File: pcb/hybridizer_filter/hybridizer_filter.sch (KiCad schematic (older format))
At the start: 107 parts, among them P1 HEADER_02X07_SMD, P2 HEADER_02X05_SMD, P3 HEADER_02X05_SMD, U1 VA, U11 VA, U13 VA, U15 DRV103, U16 DRV103, U17 DRV103, U18 DRV103, U19 DRV103, U20 DRV103, U21 DRV103, U22 DRV103, U23 OA, U24 OA, U25 OA, U26 OA, U27 OA, U28 OA, U29 OA, U3 VA, U5 VA, U7 VA, U9 VA

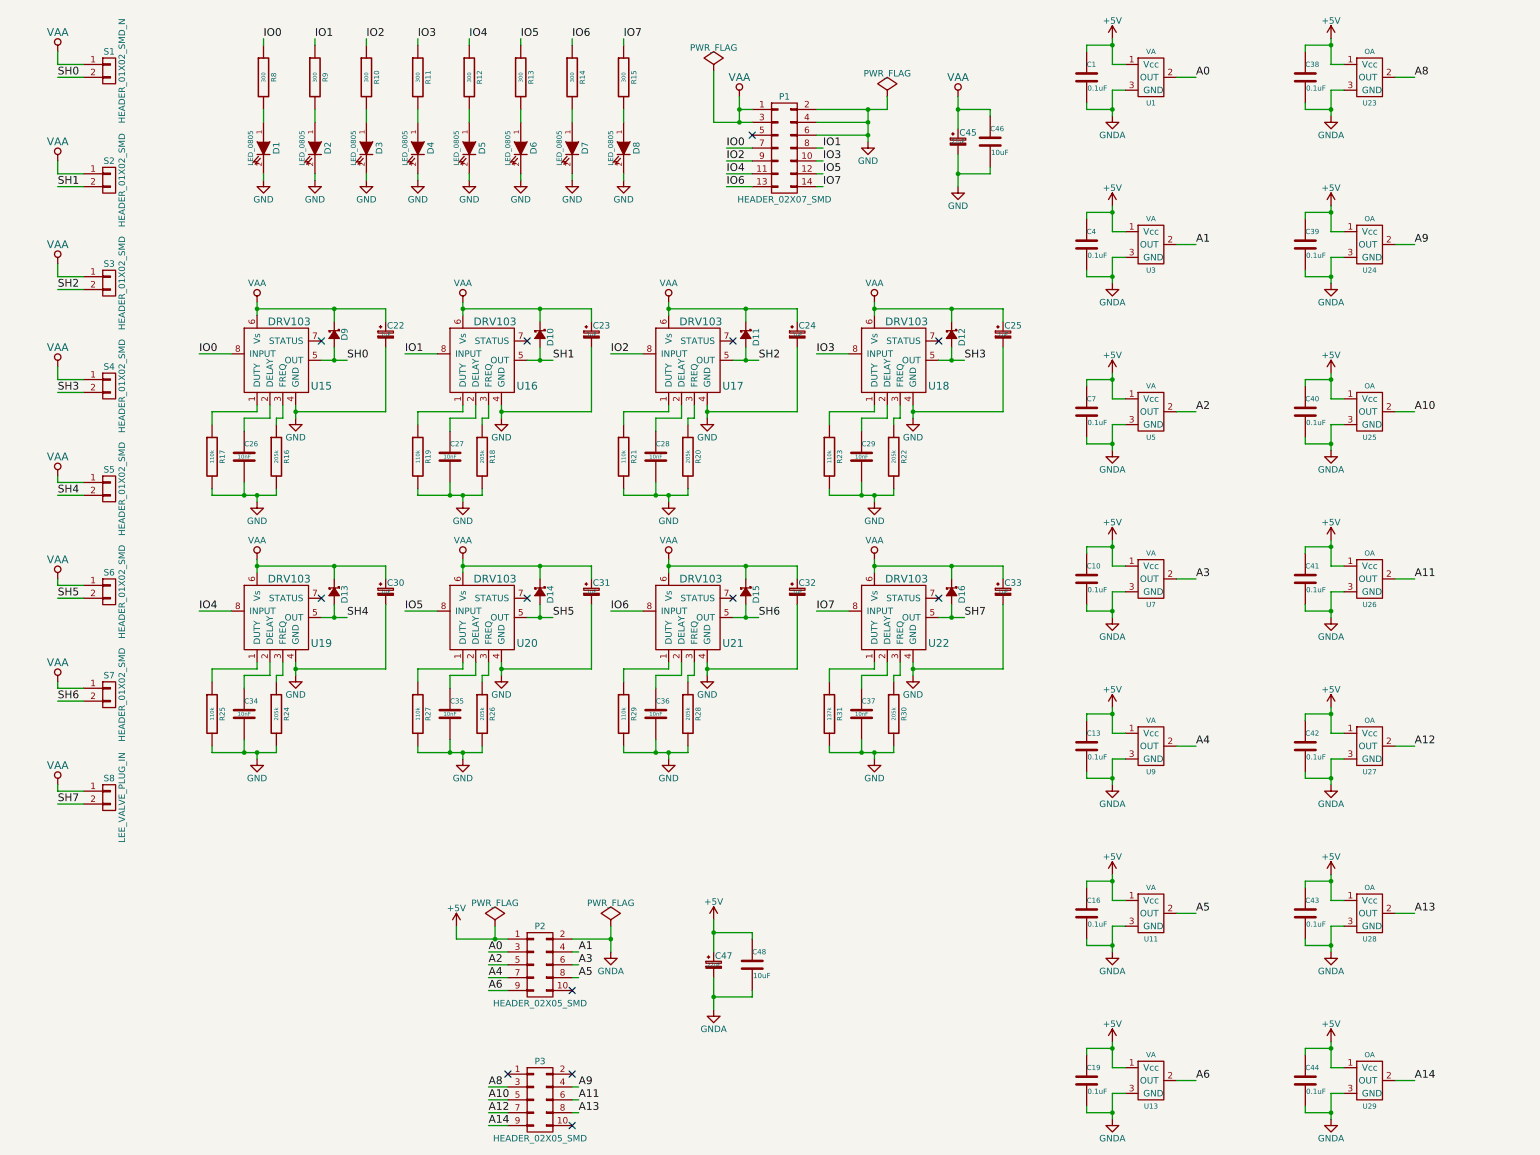
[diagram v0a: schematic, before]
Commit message: Initial design of hybridizer_filter pcb.
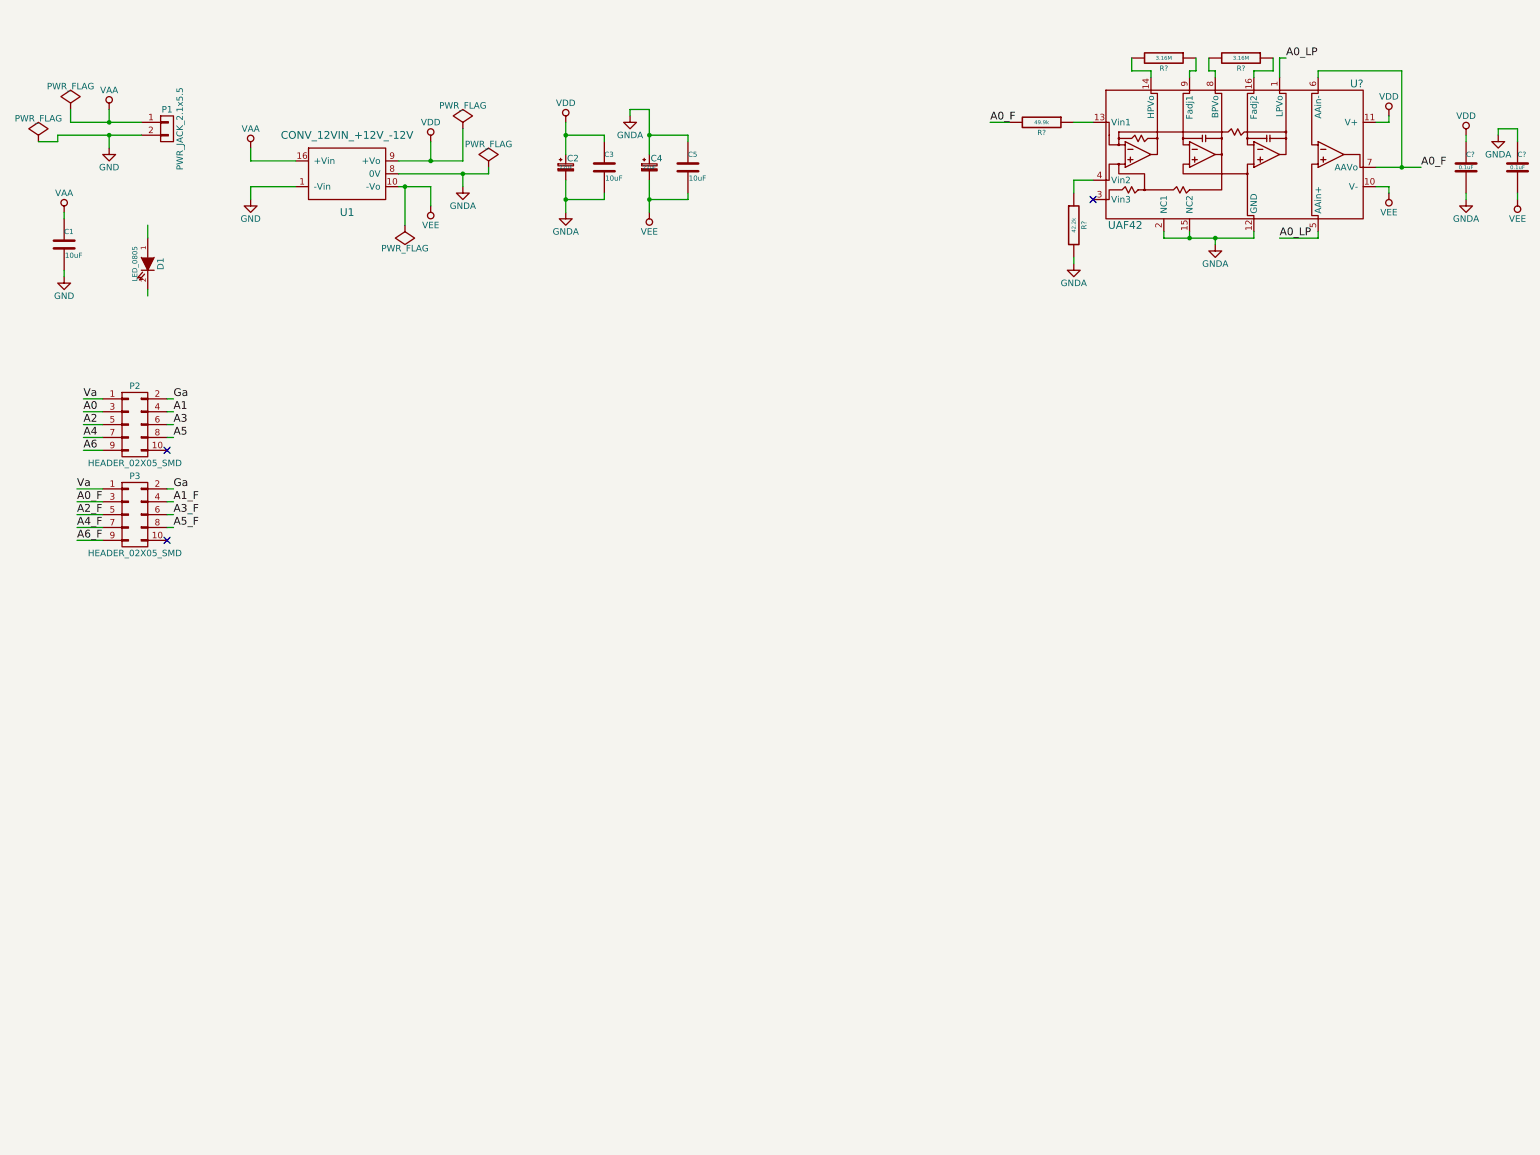
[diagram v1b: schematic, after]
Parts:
- removed C1, C10, C13, C16, C19, C38, C39, C4, C40, C41, C42, C43, C44, C7: 0.1uF, hybridizer_filter:SM1210, symbol 0.1uF
- removed C22, C23, C24, C25, C30, C31, C32, C33: 1uF, hybridizer_filter:SM0805_POL_L, symbol 1uF_0805_POL
- removed C26, C27, C28, C29, C34, C35, C36, C37: 10nF, hybridizer_filter:SM0402, symbol 10nF_0402
- removed C45: 22uF, hybridizer_filter:SM1210_POL, symbol 22uF_1210_POL
- removed C46: 10uF, hybridizer_filter:SM1210, symbol 10uF
- removed D10, D11, D12, D13, D14, D15, D16, D9: diode_schottky_20V_1A, hybridizer_filter:SM0805_POL, symbol diode_schottky_20V_1A
- removed D2, D3, D4, D5, D6, D7, D8: LED_0805, hybridizer_filter:LED0805, symbol LED_0805
- removed P1: HEADER_02X07_SMD, hybridizer_filter:HEADER_02x07_SMD, symbol HEADER_02X07_SMD
- removed R10, R11, R12, R13, R14, R15, R8, R9: 300, hybridizer_filter:SM0402, symbol 300_0402
- removed R16, R18, R20, R22, R24, R26, R28, R30: 205k, hybridizer_filter:SM0402, symbol 205k_0402
- removed R17, R19, R21, R23, R25, R27, R29: 110k, hybridizer_filter:SM0402, symbol 110k_0402
- removed R31: 137k, hybridizer_filter:SM0402, symbol 137k_0402
- removed S1: HEADER_01X02_SMD_N, hybridizer_filter:Header_2_Pin_SMD_N, symbol HEADER_01X02_SMD_N
- removed S2, S3, S4, S5, S6, S7: HEADER_01X02_SMD, hybridizer_filter:Header_2_Pin_SMD, symbol HEADER_01X02_SMD
- removed S8: LEE_VALVE_PLUG_IN, hybridizer_filter:LEE_VALVE_PLUG_IN, symbol LEE_VALVE_PLUG_IN
- removed U1, U11, U13, U3, U5, U7, U9: VA, hybridizer_filter:SOT-23-3, symbol HALL_DRV5053_VA_-9mT
- removed U15, U16, U17, U18, U19, U20, U21, U22: DRV103, hybridizer_filter:SOIC_8, symbol DRV103
- removed U23, U24, U25, U26, U27, U28, U29: OA, hybridizer_filter:SOT-23-3, symbol HALL_DRV5053_OA_-73mT
- added C1, C5: 10uF, hybridizer_filter:SM1210, symbol 10uF
- added C4: 22uF, hybridizer_filter:SM1210_POL, symbol 22uF_1210_POL
- added C? (x2): 0.1uF, hybridizer_filter:SM0805, symbol 0.1uF_0805
- added P1: PWR_JACK_2.1x5.5, hybridizer_filter:DCJACK_2PIN_HIGHCURRENT, symbol PWR_JACK_2.1x5.5
- added R?: 42.2k, hybridizer_filter:SM0805, symbol 42.2k_0805
- added R?: 49.9k, hybridizer_filter:SM0805, symbol 49.9k_0805
- added R? (x2): 3.16M, hybridizer_filter:SM0805, symbol 3.16M_0805
- added U1: CONV_12VIN_+12V_-12V, hybridizer_filter:XP_DC_DC_ISP, symbol CONV_12VIN_+12V_-12V
- added U?: UAF42, hybridizer_filter:SOIC_16, symbol UAF42
- renumbered C47 to C2, C48 to C3
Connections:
- net GND: now also C1.2, P1.2 (P2), U1.1 (-Vin); no longer D1.2 (K)
- net GNDA: now also C4.1, C5.1, C?.1, C?.2, R?.2, U1.8 (0V), U?.12 (GND), U?.15 (NC2), U?.2 (NC1); no longer P2.2 (P2)
- net VAA: now also C1.1, P1.1 (P1), U1.16 (+Vin)
- net Va: now reaches P3.1 (P1)
- net Va: now also P2.1 (P1)
- net Ga: now reaches P3.2 (P2)
- net Ga: now also P2.2 (P2)
- net +5V renamed VDD
- net VDD: now also C?.1, U1.9 (+Vo), U?.11 (V+); no longer P2.1 (P1)
- net A10 renamed A2_F
- net A11 renamed A3_F
- net A12 renamed A4_F
- net A13 renamed A5_F
- net A14 renamed A6_F
- net A8 renamed A0_F
- net A0_F: now also R?.2, U?.6 (AAin-), U?.7 (AAVo)
- net A9 renamed A1_F
- new net: R?.1, U?.13 (Vin1)
- new net: R?.2, U?.14 (HPVo)
- new net: R?.1, U?.16 (Fadj2)
- new net: R?.1, U?.4 (Vin2)
- new net: R?.2, U?.8 (BPVo)
- new net: R?.1, U?.9 (Fadj1)
- new net A0_LP: U?.1 (LPVo), U?.5 (AAin+)
- new net VEE: C4.2, C5.2, C?.2, U1.10 (-Vo), U?.10 (V-)
- no-connect marks 13 -> 3
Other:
- moved on the sheet: C2, C3, D1, P2, P3

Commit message: Progress towards hybridizer_filter v1.0.
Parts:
- removed U1: CONV_12VIN_+12V_-12V, hybridizer_filter:XP_DC_DC_ISP, symbol CONV_12VIN_+12V_-12V
- added C10, C11, C12, C13, C14, C15, C16, C17, C18, C19, C20, C21, C22, C23, C24, C25, C26, C27, C28, C29, C30, C31, C32, C33, C8, C9: 0.1uF, hybridizer_filter:SM0805, symbol 0.1uF_0805
- added P4, P5: HEADER_02X05_SMD, hybridizer_filter:HEADER_02x05_SMD, symbol HEADER_02X05_SMD
- added R1: 1k, hybridizer_filter:SM0805, symbol 1k_0805
- added R10, R11, R14, R15, R18, R19, R22, R23, R26, R27, R30, R31, R34, R35, R38, R39, R42, R43, R46, R47, R50, R51, R54, R55, R6, R7: 3.16M, hybridizer_filter:SM0805, symbol 3.16M_0805
- added R12, R16, R20, R24, R28, R32, R36, R40, R44, R48, R52, R56, R8: 49.9k, hybridizer_filter:SM0805, symbol 49.9k_0805
- added R13, R17, R21, R25, R29, R33, R37, R41, R45, R49, R53, R57, R9: 42.2k, hybridizer_filter:SM0805, symbol 42.2k_0805
- added U1: CONV_+9V_-9V_SIP8, hybridizer_filter:SIP8_RECOM, symbol CONV_+9V_-9V_SIP8
- added U10, U11, U12, U13, U14, U15, U3, U4, U5, U6, U7, U8, U9: UAF42, hybridizer_filter:SOIC_16, symbol UAF42
- gave numbers to parts that had none: 7
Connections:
- net Ga is gone; now on net GNDA: P2.2 (P2), P3.2 (P2)
- net A0: now also R4.2
- net A0_F: no longer R4.2
- net A1: now also R8.2
- net A1_F: now also U3.6 (AAin-), U3.7 (AAVo)
- net A2: now also R12.2
- net A2_F: now also U4.6 (AAin-), U4.7 (AAVo)
- net A3: now also R16.2
- net A3_F: now also U5.6 (AAin-), U5.7 (AAVo)
- net A4: now also R20.2
- net A4_F: now also U6.6 (AAin-), U6.7 (AAVo)
- net A5: now also R24.2
- net A5_F: now also U7.6 (AAin-), U7.7 (AAVo)
- net A6: now also R28.2
- net A6_F: now also U8.6 (AAin-), U8.7 (AAVo)
- net GND: now also D1.2 (K), U1.1 (-Vin)
- net GNDA: now also C10.2, C11.1, C12.2, C13.1, C14.2, C15.1, C16.2, C17.1, C18.2, C19.1, C20.2, C21.1, C22.2, C23.1, C24.2, C25.1, C26.2, C27.1, C28.2, C29.1, C30.2, C31.1, C32.2, C33.1, C8.2, C9.1, R13.2, R17.2, R21.2, R25.2, R29.2, R33.2, R37.2, R41.2, R45.2, R49.2, R53.2, R57.2, R9.2, U1.7 (COM), U10.12 (GND), U10.15 (NC2), U10.2 (NC1), U11.12 (GND), U11.15 (NC2), U11.2 (NC1), U12.12 (GND), U12.15 (NC2), U12.2 (NC1), U13.12 (GND), U13.15 (NC2), U13.2 (NC1), U14.12 (GND), U14.15 (NC2), U14.2 (NC1), U15.12 (GND), U15.15 (NC2), U15.2 (NC1), U3.12 (GND), U3.15 (NC2), U3.2 (NC1), U4.12 (GND), U4.15 (NC2), U4.2 (NC1), U5.12 (GND), U5.15 (NC2), U5.2 (NC1), U6.12 (GND), U6.15 (NC2), U6.2 (NC1), U7.12 (GND), U7.15 (NC2), U7.2 (NC1), U8.12 (GND), U8.15 (NC2), U8.2 (NC1), U9.12 (GND), U9.15 (NC2), U9.2 (NC1)
- net VAA: now also R1.1, U1.2 (+Vin)
- net VDD: now also C10.1, C12.1, C14.1, C16.1, C18.1, C20.1, C22.1, C24.1, C26.1, C28.1, C30.1, C32.1, C8.1, U1.6 (+Vo), U10.11 (V+), U11.11 (V+), U12.11 (V+), U13.11 (V+), U14.11 (V+), U15.11 (V+), U3.11 (V+), U4.11 (V+), U5.11 (V+), U6.11 (V+), U7.11 (V+), U8.11 (V+), U9.11 (V+)
- net VEE: now also C11.2, C13.2, C15.2, C17.2, C19.2, C21.2, C23.2, C25.2, C27.2, C29.2, C31.2, C33.2, C9.2, U1.8 (-Vo), U10.10 (V-), U11.10 (V-), U12.10 (V-), U13.10 (V-), U14.10 (V-), U15.10 (V-), U3.10 (V-), U4.10 (V-), U5.10 (V-), U6.10 (V-), U7.10 (V-), U8.10 (V-), U9.10 (V-)
- net at D1.1 (A): now also R1.2
- new net: R8.1, U3.13 (Vin1)
- new net: R6.2, U3.14 (HPVo)
- new net: R7.1, U3.16 (Fadj2)
- new net: R9.1, U3.4 (Vin2)
- new net: R7.2, U3.8 (BPVo)
- new net: R6.1, U3.9 (Fadj1)
- new net: R12.1, U4.13 (Vin1)
- new net: R10.2, U4.14 (HPVo)
- new net: R11.1, U4.16 (Fadj2)
- new net: R13.1, U4.4 (Vin2)
- new net: R11.2, U4.8 (BPVo)
- new net: R10.1, U4.9 (Fadj1)
- new net: R16.1, U5.13 (Vin1)
- new net: R14.2, U5.14 (HPVo)
- new net: R15.1, U5.16 (Fadj2)
- new net: R17.1, U5.4 (Vin2)
- new net: R15.2, U5.8 (BPVo)
- new net: R14.1, U5.9 (Fadj1)
- new net: R20.1, U6.13 (Vin1)
- new net: R18.2, U6.14 (HPVo)
- new net: R19.1, U6.16 (Fadj2)
- new net: R21.1, U6.4 (Vin2)
- new net: R19.2, U6.8 (BPVo)
- new net: R18.1, U6.9 (Fadj1)
- new net: R24.1, U7.13 (Vin1)
- new net: R22.2, U7.14 (HPVo)
- new net: R23.1, U7.16 (Fadj2)
- new net: R25.1, U7.4 (Vin2)
- new net: R23.2, U7.8 (BPVo)
- new net: R22.1, U7.9 (Fadj1)
- new net: R28.1, U8.13 (Vin1)
- new net: R26.2, U8.14 (HPVo)
- new net: R27.1, U8.16 (Fadj2)
- new net: R29.1, U8.4 (Vin2)
- new net: R27.2, U8.8 (BPVo)
- new net: R26.1, U8.9 (Fadj1)
- new net: R32.1, U9.13 (Vin1)
- new net: R30.2, U9.14 (HPVo)
- new net: R31.1, U9.16 (Fadj2)
- new net: R33.1, U9.4 (Vin2)
- new net: R31.2, U9.8 (BPVo)
- new net: R30.1, U9.9 (Fadj1)
- new net: R36.1, U10.13 (Vin1)
- new net: R34.2, U10.14 (HPVo)
- new net: R35.1, U10.16 (Fadj2)
- new net: R37.1, U10.4 (Vin2)
- new net: R35.2, U10.8 (BPVo)
- new net: R34.1, U10.9 (Fadj1)
- new net: R40.1, U11.13 (Vin1)
- new net: R38.2, U11.14 (HPVo)
- new net: R39.1, U11.16 (Fadj2)
- new net: R41.1, U11.4 (Vin2)
- new net: R39.2, U11.8 (BPVo)
- new net: R38.1, U11.9 (Fadj1)
- new net: R44.1, U12.13 (Vin1)
- new net: R42.2, U12.14 (HPVo)
- new net: R43.1, U12.16 (Fadj2)
- new net: R45.1, U12.4 (Vin2)
- new net: R43.2, U12.8 (BPVo)
- new net: R42.1, U12.9 (Fadj1)
- new net: R48.1, U13.13 (Vin1)
- new net: R46.2, U13.14 (HPVo)
- new net: R47.1, U13.16 (Fadj2)
- new net: R49.1, U13.4 (Vin2)
- new net: R47.2, U13.8 (BPVo)
- new net: R46.1, U13.9 (Fadj1)
- new net: R52.1, U14.13 (Vin1)
- new net: R50.2, U14.14 (HPVo)
- new net: R51.1, U14.16 (Fadj2)
- new net: R53.1, U14.4 (Vin2)
- new net: R51.2, U14.8 (BPVo)
- new net: R50.1, U14.9 (Fadj1)
- new net: R56.1, U15.13 (Vin1)
- new net: R54.2, U15.14 (HPVo)
- new net: R55.1, U15.16 (Fadj2)
- new net: R57.1, U15.4 (Vin2)
- new net: R55.2, U15.8 (BPVo)
- new net: R54.1, U15.9 (Fadj1)
- new net A10: P4.5 (P5), R40.2
- new net A10_F: P5.5 (P5), U11.6 (AAin-), U11.7 (AAVo)
- new net A10_LP: U11.1 (LPVo), U11.5 (AAin+)
- new net A11: P4.6 (P6), R44.2
- new net A11_F: P5.6 (P6), U12.6 (AAin-), U12.7 (AAVo)
- new net A11_LP: U12.1 (LPVo), U12.5 (AAin+)
- new net A12: P4.7 (P7), R48.2
- new net A12_F: P5.7 (P7), U13.6 (AAin-), U13.7 (AAVo)
- new net A12_LP: U13.1 (LPVo), U13.5 (AAin+)
- new net A13: P4.8 (P8), R52.2
- new net A13_F: P5.8 (P8), U14.6 (AAin-), U14.7 (AAVo)
- new net A13_LP: U14.1 (LPVo), U14.5 (AAin+)
- new net A14: P4.9 (P9), R56.2
- new net A14_F: P5.9 (P9), U15.6 (AAin-), U15.7 (AAVo)
- new net A14_LP: U15.1 (LPVo), U15.5 (AAin+)
- new net A1_LP: U3.1 (LPVo), U3.5 (AAin+)
- new net A2_LP: U4.1 (LPVo), U4.5 (AAin+)
- new net A3_LP: U5.1 (LPVo), U5.5 (AAin+)
- new net A4_LP: U6.1 (LPVo), U6.5 (AAin+)
- new net A5_LP: U7.1 (LPVo), U7.5 (AAin+)
- new net A6_LP: U8.1 (LPVo), U8.5 (AAin+)
- new net A8: P4.3 (P3), R32.2
- new net A8_F: P5.3 (P3), U9.6 (AAin-), U9.7 (AAVo)
- new net A8_LP: U9.1 (LPVo), U9.5 (AAin+)
- new net A9: P4.4 (P4), R36.2
- new net A9_F: P5.4 (P4), U10.6 (AAin-), U10.7 (AAVo)
- new net A9_LP: U10.1 (LPVo), U10.5 (AAin+)
- new net Gb: P4.2 (P2), P5.2 (P2)
- new net Vb: P4.1 (P1), P5.1 (P1)
- no-connect marks 3 -> 18
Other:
- moved on the sheet: D1, P3

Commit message: Partial correction to an incorrect value.
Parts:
- removed R13, R17, R21, R25, R29, R33, R37, R41, R45, R49, R5, R53, R57, R9: 42.2k, hybridizer_filter:SM0805, symbol 42.2k_0805
- added R13, R17, R21, R25, R29, R33, R37, R41, R45, R49, R5, R53, R57, R9: 44.2k, hybridizer_filter:SM0805, symbol 44.2k_0805
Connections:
- net GNDA: now also R13.2, R17.2, R21.2, R25.2, R29.2, R33.2, R37.2, R41.2, R45.2, R49.2, R5.2, R53.2, R57.2, R9.2
- net at U2.4 (Vin2): now also R5.1
- net at U3.4 (Vin2): now also R9.1
- net at U4.4 (Vin2): now also R13.1
- net at U5.4 (Vin2): now also R17.1
- net at U6.4 (Vin2): now also R21.1
- net at U7.4 (Vin2): now also R25.1
- net at U8.4 (Vin2): now also R29.1
- net at U9.4 (Vin2): now also R33.1
- net at U10.4 (Vin2): now also R37.1
- net at U11.4 (Vin2): now also R41.1
- net at U12.4 (Vin2): now also R45.1
- net at U13.4 (Vin2): now also R49.1
- net at U14.4 (Vin2): now also R53.1
- net at U15.4 (Vin2): now also R57.1
